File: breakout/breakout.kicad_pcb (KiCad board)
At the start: 4 copper layers, 99.5 x 80 mm, 141 parts, among them J1 M20-9982046, J10 B3B-XH-A, J11 B3B-XH-A, J12 B3B-XH-A, J4 B3B-XH-A, J5 B3B-XH-A, J6 B2B-XH-A, J7 B3B-XH-A, J8 B3B-XH-A, J9 B3B-XH-A, Q1 AO3401A, U1 74LVC32APW,118, U10 MCP251863T-E/SS, U11 MCP251863T-E/SS, U12 MCP251863T-E/SS, U13 MCP251863T-E/SS, U14 MCP251863T-E/SS, U15 MCP251863T-E/SS, U16 MCP251863T-E/SS, U2 74LVC04AT14-13, U3 TLV75533PDBVR, U4 74AHC30PW,118, U5 74LVC32APW,118, U9 MCP251863T-E/SS, Y1 ABM8G-40.000MHZ-18-D2Y-T, Y2 ABM8G-40.000MHZ-18-D2Y-T, Y3 ABM8G-40.000MHZ-18-D2Y-T, Y4 ABM8G-40.000MHZ-18-D2Y-T, Y5 ABM8G-40.000MHZ-18-D2Y-T, Y6 ABM8G-40.000MHZ-18-D2Y-T, Y7 ABM8G-40.000MHZ-18-D2Y-T, Y8 ABM8G-40.000MHZ-18-D2Y-T

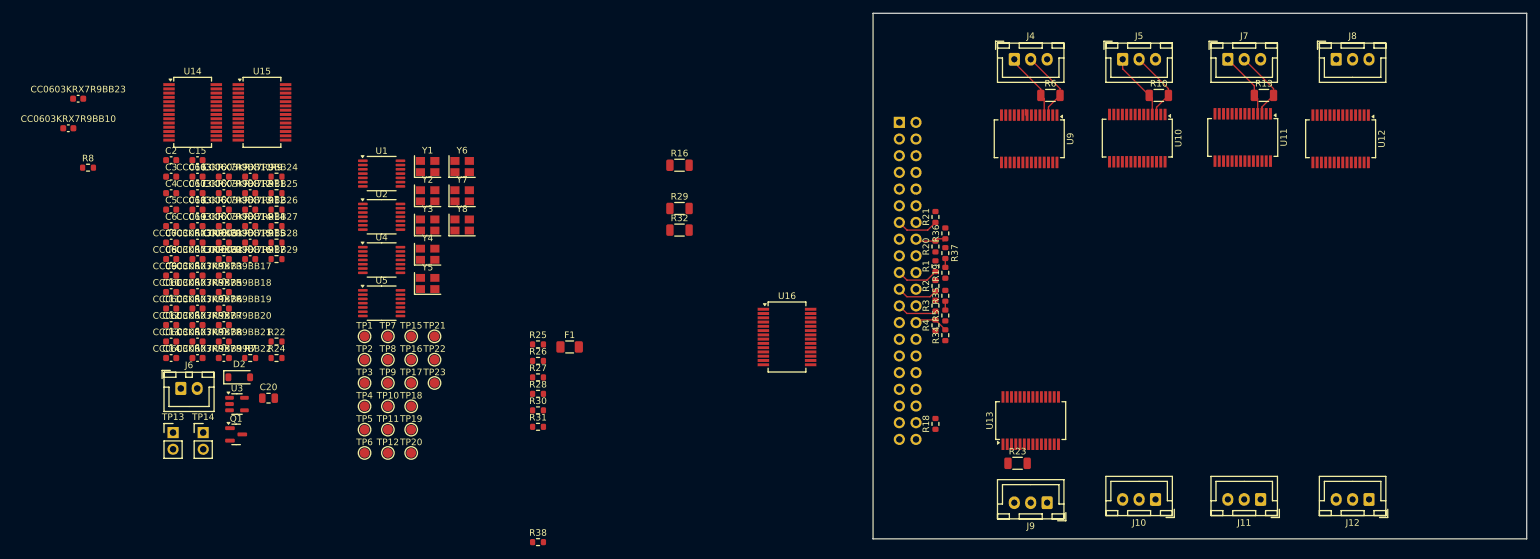
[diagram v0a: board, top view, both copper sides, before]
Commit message: Complete compact four-layer SPI-to-CAN board layout
Arrange all 141 components on a 77 x 80 mm board, route every connection,
place bypass capacitors beside their IC supply pins, and keep oscillator
signals on the front copper without vias. Shorten SPI clock routes and
document the layer use and route measurements.

Keep schematic/ERC project settings, use portable project library paths,
and remove two stray no-connect markers. Stop tracking KiCad lock files,
local preferences and session history; ignore editor state and backups.

Validation: KiCad 10.0.7 reports zero DRC violations, zero unconnected
items, and zero schematic/PCB parity issues.
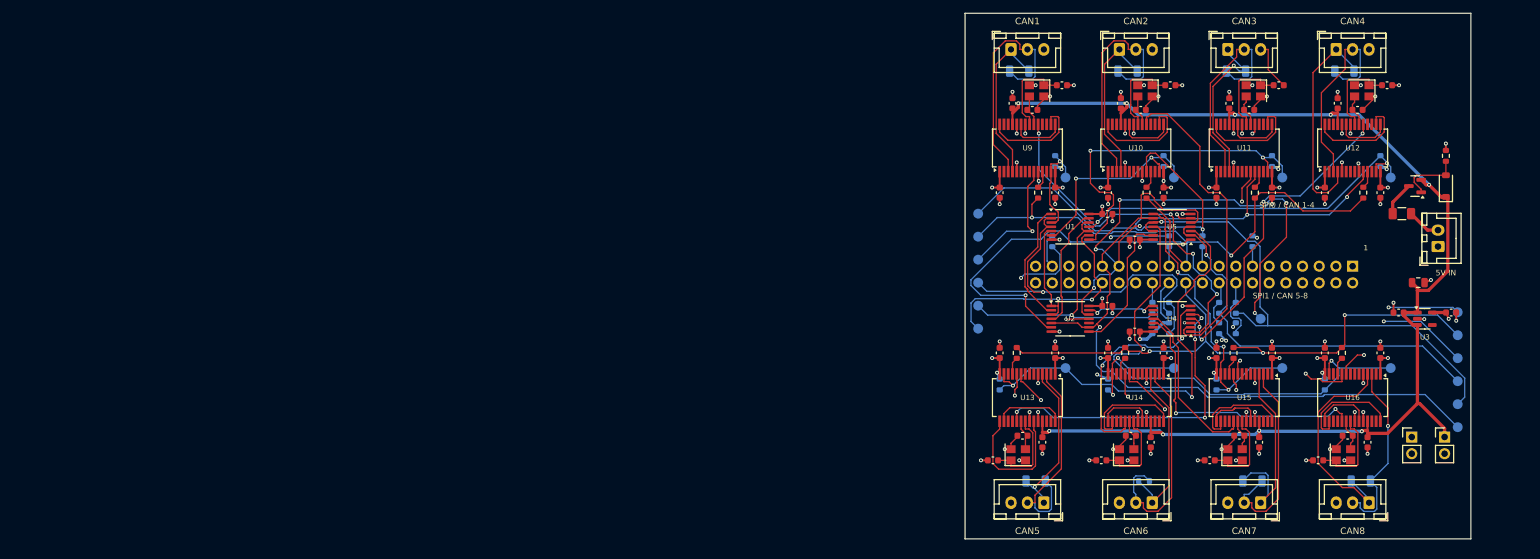
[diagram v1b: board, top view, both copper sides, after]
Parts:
- R1, R10, R11, R13, R14, R16, R17, R18, R19, R20, R21, R23, R24, R26, R27, R29, R3, R30, R32, R34, R35, R36, R37, R4, R5, R6, R7, R8, TP1, TP10, TP11, TP12, TP15, TP16, TP17, TP18, TP19, TP2, TP20, TP21, TP22, TP23, TP3, TP4, TP5, TP6, TP7, TP8, TP9: moved to B.Cu
- moved J6 192.6 mm to (132.0, 83.0), turned to 90 degrees
- moved C19 191.3 mm to (134.0, 93.0), turned to 180 degrees
- moved TP14 189.0 mm to (133.0, 112.0)
- moved TP13 188.6 mm to (128.0, 112.0)
- moved C9 187.3 mm to (124.2, 58.5)
- moved D2 186.0 mm to (133.2, 73.8), turned to 90 degrees
- moved C18 183.5 mm to (126.0, 93.0)
- moved Q1 183.4 mm to (128.5, 73.8), turned to 180 degrees
- moved C8 182.0 mm to (119.8, 62.2), turned to 180 degrees
- moved U3 181.3 mm to (130.0, 94.0)
- moved C16 179.5 mm to (118.2, 111.8)
- moved CC0603KRX7R9BB15 176.2 mm to (123.2, 74.8), turned to 90 degrees
- moved C20 175.9 mm to (129.0, 88.5)
- moved C17 175.4 mm to (113.8, 115.5), turned to 180 degrees
- moved CC0603KRX7R9BB27 173.1 mm to (123.2, 99.2), turned to 90 degrees
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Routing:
- net VCC: track 0.00 -> 206.0 mm, vias 0 -> 9
- net SPI1_MOSI: track 0.00 -> 155.0 mm, vias 0 -> 6
- net GND: track 0.00 -> 123.4 mm, vias 0 -> 84
- net SPI1_SCK: track 0.00 -> 115.1 mm, vias 0 -> 6
- net GPIO_11: track 0.00 -> 111.9 mm, vias 0 -> 1
- net SPI0_MOSI: track 0.00 -> 107.6 mm, vias 0 -> 4
- net SPI0_SCK: track 0.00 -> 106.9 mm, vias 0 -> 5
- net VDD_VIO: track 0.00 -> 94.6 mm, vias 0 -> 33
- net SPI1_MISO: track 0.00 -> 90.9 mm, vias 0 -> 3
- net SPI0_MISO: track 6.32 -> 91.5 mm, vias 0 -> 2
- net GPIO_1: track 0.00 -> 79.9 mm, vias 0 -> 6
- net CAN8_CS: track 0.00 -> 77.5 mm, vias 0 -> 2
- net SPI1_CS1: track 0.00 -> 76.8 mm, vias 0 -> 1
- net CAN5_CS: track 0.00 -> 65.6 mm, vias 0 -> 2
- net SPI1_CS0: track 0.00 -> 60.2 mm, vias 0 -> 1
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- added copper zone on In2.Cu, net VDD_VIO
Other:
- board size 99.5 x 80 mm -> 77 x 80 mm
- board text added: "1"
- board text added: "5V IN"
- board text added: "CAN1"
- board text added: "CAN2"
- board text added: "CAN3"
- board text added: "CAN4"
- board text added: "CAN5"
- board text added: "CAN6"
- board text added: "CAN7"
- board text added: "CAN8"
- board text added: "JETSON SPI - 8x CAN FD"
- board text added: "SPI0 / CAN 1-4"
- board text added: "SPI1 / CAN 5-8"

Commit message: Connect all Jetson J1 ground pins in schematic and PCB
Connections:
- J1 pad 14: unconnected-(J1-Pin_14-Pad14) -> GND
- J1 pad 20: unconnected-(J1-Pin_20-Pad20) -> GND
- J1 pad 25: unconnected-(J1-Pin_25-Pad25) -> GND
- J1 pad 30: unconnected-(J1-Pin_30-Pad30) -> GND
- J1 pad 34: unconnected-(J1-Pin_34-Pad34) -> GND
- J1 pad 6: unconnected-(J1-Pin_6-Pad6) -> GND
- J1 pad 9: unconnected-(J1-Pin_9-Pad9) -> GND
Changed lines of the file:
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@@
 			(layers "*.Cu" "*.Mask")
 			(remove_unused_layers no)
-			(net "unconnected-(J1-Pin_6-Pad6)")
+			(net "GND")
 			(pinfunction "Pin_6_6")
-			(pintype "passive+no_connect")
+			(pintype "passive")
 		)
 		(pad "7" thru_hole circle
@@
 			(layers "*.Cu" "*.Mask")
 			(remove_unused_layers no)
-			(net "unconnected-(J1-Pin_9-Pad9)")
+			(net "GND")
 			(pinfunction "Pin_9_9")
-			(pintype "passive+no_connect")
+			(pintype "passive")
 		)
 		(pad "10" thru_hole circle
@@
 			(layers "*.Cu" "*.Mask")
 			(remove_unused_layers no)
-			(net "unconnected-(J1-Pin_14-Pad14)")
+			(net "GND")
 			(pinfunction "Pin_14_14")
-			(pintype "passive+no_connect")
+			(pintype "passive")
 		)
 		(pad "15" thru_hole circle
@@
 			(layers "*.Cu" "*.Mask")
 			(remove_unused_layers no)
-			(net "unconnected-(J1-Pin_20-Pad20)")
+			(net "GND")
 			(pinfunction "Pin_20_20")
-			(pintype "passive+no_connect")
+			(pintype "passive")
 		)
 		(pad "21" thru_hole circle
@@
 			(layers "*.Cu" "*.Mask")
 			(remove_unused_layers no)
-			(net "unconnected-(J1-Pin_25-Pad25)")
+			(net "GND")
 			(pinfunction "Pin_25_25")
-			(pintype "passive+no_connect")
+			(pintype "passive")
 		)
 		(pad "26" thru_hole circle
@@
 			(layers "*.Cu" "*.Mask")
 			(remove_unused_layers no)
-			(net "unconnected-(J1-Pin_30-Pad30)")
+			(net "GND")
 			(pinfunction "Pin_30_30")
-			(pintype "passive+no_connect")
+			(pintype "passive")
 		)
 		(pad "31" thru_hole circle
@@
 			(layers "*.Cu" "*.Mask")
 			(remove_unused_layers no)
-			(net "unconnected-(J1-Pin_34-Pad34)")
+			(net "GND")
 			(pinfunction "Pin_34_34")
-			(pintype "passive+no_connect")
+			(pintype "passive")
 		)
 		(pad "35" thru_hole circle

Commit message: fixed footprints, created orderlist, added mounting holes
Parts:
- added H1: M3 mounting hole, MountingHole_3.2mm_M3_7mm_Keepout, F.Cu at (60.0, 51.5)
- added H2: M3 mounting hole, MountingHole_3.2mm_M3_7mm_Keepout, F.Cu at (133.0, 51.5)
- added H3: M3 mounting hole, MountingHole_3.2mm_M3_7mm_Keepout, F.Cu at (60.0, 123.5)
- added H4: M3 mounting hole, MountingHole_3.2mm_M3_7mm_Keepout, F.Cu at (133.0, 123.5)
- C1: renamed from CC0603KRX7R9BB1; value CC0603KRX7R9BB104 -> 100n
- C21: renamed from CC0603KRX7R9BB2; value CC0603KRX7R9BB104 -> 100n
- C22: renamed from CC0603KRX7R9BB3; value CC0603KRX7R9BB104 -> 100n
- C23: renamed from CC0603KRX7R9BB5; value CC0603KRX7R9BB104 -> 100n
- C24: renamed from CC0603KRX7R9BB6; value CC0603KRX7R9BB104 -> 100n
- C25: renamed from CC0603KRX7R9BB7; value CC0603KRX7R9BB104 -> 100n
- C26: renamed from CC0603KRX7R9BB8; value CC0603KRX7R9BB104 -> 100n
- C27: renamed from CC0603KRX7R9BB9; value CC0603KRX7R9BB104 -> 100n
- C28: renamed from CC0603KRX7R9BB10; value CC0603KRX7R9BB104 -> 100n
- C29: renamed from CC0603KRX7R9BB11; value CC0603KRX7R9BB104 -> 100n
- C30: renamed from CC0603KRX7R9BB12; value CC0603KRX7R9BB104 -> 100n
- C31: renamed from CC0603KRX7R9BB13; value CC0603KRX7R9BB104 -> 100n
- C32: renamed from CC0603KRX7R9BB14; value CC0603KRX7R9BB104 -> 100n
- C33: renamed from CC0603KRX7R9BB15; value CC0603KRX7R9BB104 -> 100n
- C34: renamed from CC0603KRX7R9BB16; value CC0603KRX7R9BB104 -> 100n
- C35: renamed from CC0603KRX7R9BB17; value CC0603KRX7R9BB104 -> 100n
- C36: renamed from CC0603KRX7R9BB18; value CC0603KRX7R9BB104 -> 100n
- C37: renamed from CC0603KRX7R9BB19; value CC0603KRX7R9BB104 -> 100n
- C38: renamed from CC0603KRX7R9BB20; value CC0603KRX7R9BB104 -> 100n
- C39: renamed from CC0603KRX7R9BB21; value CC0603KRX7R9BB104 -> 100n
- C40: renamed from CC0603KRX7R9BB22; value CC0603KRX7R9BB104 -> 100n
- C41: renamed from CC0603KRX7R9BB23; value CC0603KRX7R9BB104 -> 100n
- C42: renamed from CC0603KRX7R9BB24; value CC0603KRX7R9BB104 -> 100n
- C43: renamed from CC0603KRX7R9BB25; value CC0603KRX7R9BB104 -> 100n
- C44: renamed from CC0603KRX7R9BB26; value CC0603KRX7R9BB104 -> 100n
- C45: renamed from CC0603KRX7R9BB27; value CC0603KRX7R9BB104 -> 100n
- C46: renamed from CC0603KRX7R9BB28; value CC0603KRX7R9BB104 -> 100n
- C47: renamed from CC0603KRX7R9BB29; value CC0603KRX7R9BB104 -> 100n
- J1: value M20-9982046 -> M20-7832046
- R26: footprint BreakoutBoard:R_0603_1608Metric -> BreakoutBoard:R_1206_3216Metric
- TP13, TP14: value TestPoint_2Pole -> M20-9990246
- turned R26 to 180 degrees
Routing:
- net Net-(J10-Pin_2): track 33.9 -> 30.6 mm
- net Net-(J10-Pin_1): track 26.0 -> 25.2 mm
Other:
- board size 77 x 80 mm -> 81 x 80 mm
